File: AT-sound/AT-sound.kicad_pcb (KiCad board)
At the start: 2 copper layers, 17.6 x 17.6 mm, 24 parts, among them J1 PWR, J2 Sound OUT, J3 Sound IN, Q1 AQY212S, U1 ATtiny24-20SSU, U2 SFH617A-2X006, U3 SFH617A-2X006

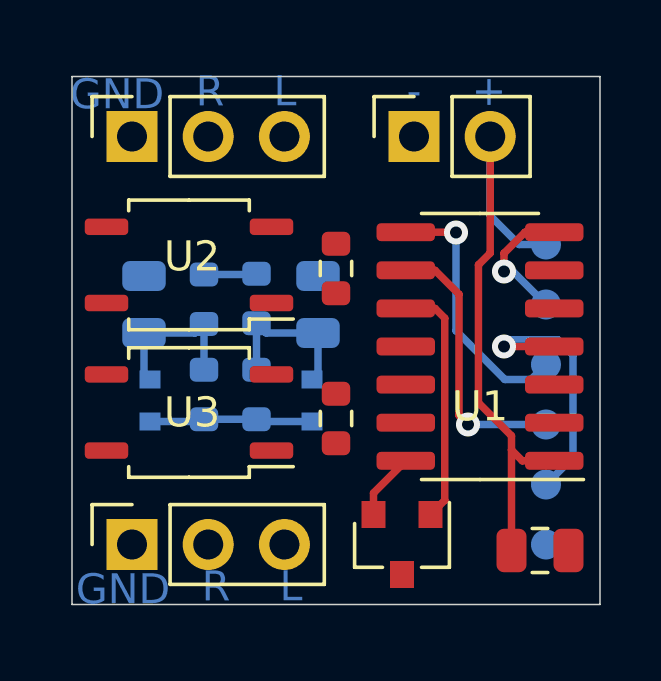
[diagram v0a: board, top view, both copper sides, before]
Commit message: made a external realay verant.
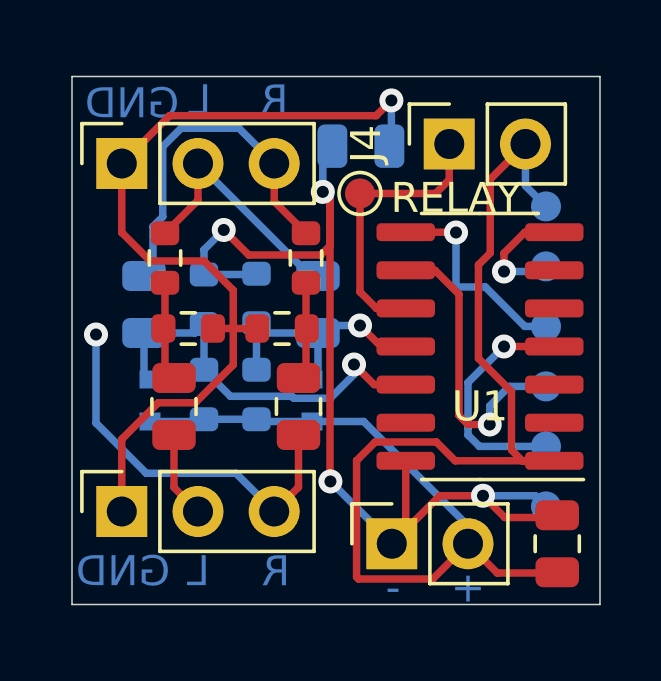
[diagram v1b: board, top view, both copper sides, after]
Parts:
- removed Q1: AQY212S, Package_TO_SOT_SMD:SOT-23
- removed U2, U3: SFH617A-2X006, Package_SO:SOP-4_3.8x4.1mm_P2.54mm
- added C4: 1uF, Capacitor_SMD:C_0805_2012Metric, F.Cu at (161.8, 70.4)
- added C5: 1uF, Capacitor_SMD:C_0805_2012Metric, F.Cu at (157.6, 70.4)
- added C6: 25uF, Capacitor_SMD:C_0805_2012Metric, B.Cu at (163.8, 61.7)
- added J4: PWR, Connector_PinSocket_2.54mm:PinSocket_1x02_P2.54mm_Vertical, F.Cu at (166.8, 61.6)
- added R7: 1K, Resistor_SMD:R_0603_1608Metric, F.Cu at (158.1, 67.8)
- added R8: 1K, Resistor_SMD:R_0603_1608Metric, F.Cu at (161.2, 67.8)
- added TP7: RELAY, TestPoint:TestPoint_Pad_D1.0mm, F.Cu at (163.8, 63.3)
- R5, R6: value 700r -> 27K
- moved J1 13.6 mm to (164.9, 75.0)
- moved J3 12.7 mm to (155.9, 62.3)
- moved J2 12.5 mm to (155.9, 73.9)
- moved R6 7.82 mm to (157.3, 65.5)
- moved TP1 1.27 mm to (170.0, 63.7)
- moved TP2 1.27 mm to (170.0, 73.7)
- moved TP3 1.27 mm to (170.0, 71.7)
- moved TP4 1.27 mm to (170.0, 69.7)
- moved TP5 1.27 mm to (170.0, 67.7)
- moved TP6 1.27 mm to (170.0, 65.7)
- moved R5 1.06 mm to (162.0, 65.5)
- moved C1 0.62 mm to (170.4, 75.0), turned to 90 degrees
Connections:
- J2 pad 1: GND -> Net-(C6-Pad1)
- J3 pad 1: GND -> Net-(C6-Pad1)
- R5 pad 1: Net-(R5-Pad1) -> Net-(C2-Pad1)
- R5 pad 2: Net-(Q1-Pad3) -> Net-(C4-Pad1)
- R6 pad 1: Net-(R6-Pad1) -> Net-(C3-Pad1)
- R6 pad 2: Net-(Q1-Pad3) -> Net-(C5-Pad1)
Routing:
- net GND: track 4.00 -> 35.7 mm, vias 0 -> 4
- net Net-(C6-Pad1): track 0.00 -> 29.3 mm, vias 0 -> 1
- net +5V: track 26.4 -> 46.5 mm
- net Net-(C4-Pad2): track 0.00 -> 13.0 mm, vias 0 -> 1
- net Net-(C2-Pad1): track 0.00 -> 11.8 mm
- net Net-(C3-Pad1): track 0.00 -> 8.33 mm
- net Sense_R: track 5.28 -> 13.3 mm, vias 0 -> 1
- net Sense_L: track 5.37 -> 8.69 mm, vias 0 -> 1
- net Net-(C5-Pad1): track 0.00 -> 3.30 mm
- net Net-(C4-Pad1): track 0.00 -> 3.28 mm
- net Net-(C5-Pad2): track 0.00 -> 2.88 mm
- net Net-(TP5-Pad1): track 8.83 -> 7.04 mm
- net Relay: track 8.18 -> 9.39 mm
- net Net-(TP3-Pad1): track 8.97 -> 7.88 mm
- net Net-(TP4-Pad1): track 9.17 -> 10.1 mm

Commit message: added my smol logo
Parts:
- added REF**: rg-logo-smol, RG:rg-logo-smol, F.Cu at (165.1, 65.5)
- TP3: value RESET -> RE
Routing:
- net (no net): track 0.00 -> 2.57 mm
- net Sense_L: track 8.69 -> 10.1 mm
- net Net-(TP5-Pad1): track 7.04 -> 6.47 mm

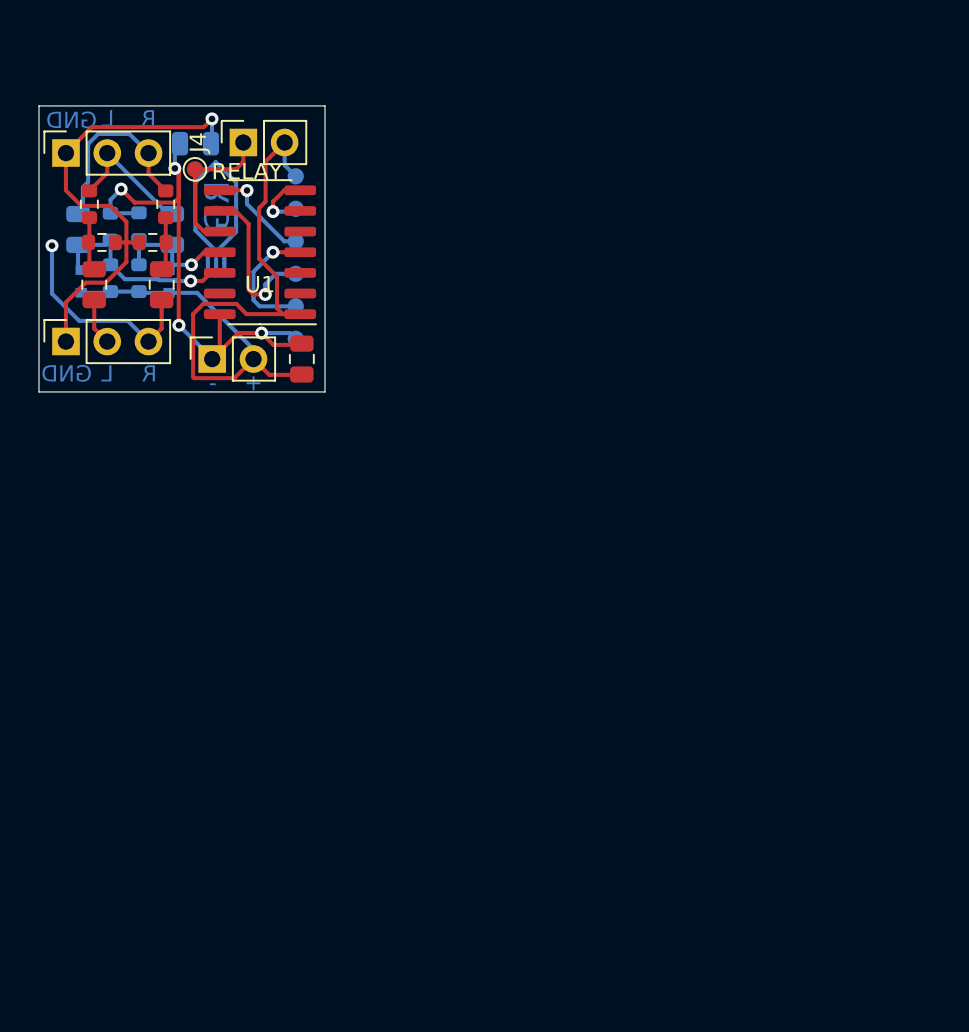
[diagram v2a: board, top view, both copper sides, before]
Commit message: added capacitive dropper cirict for POWERgit add *git add *git add *
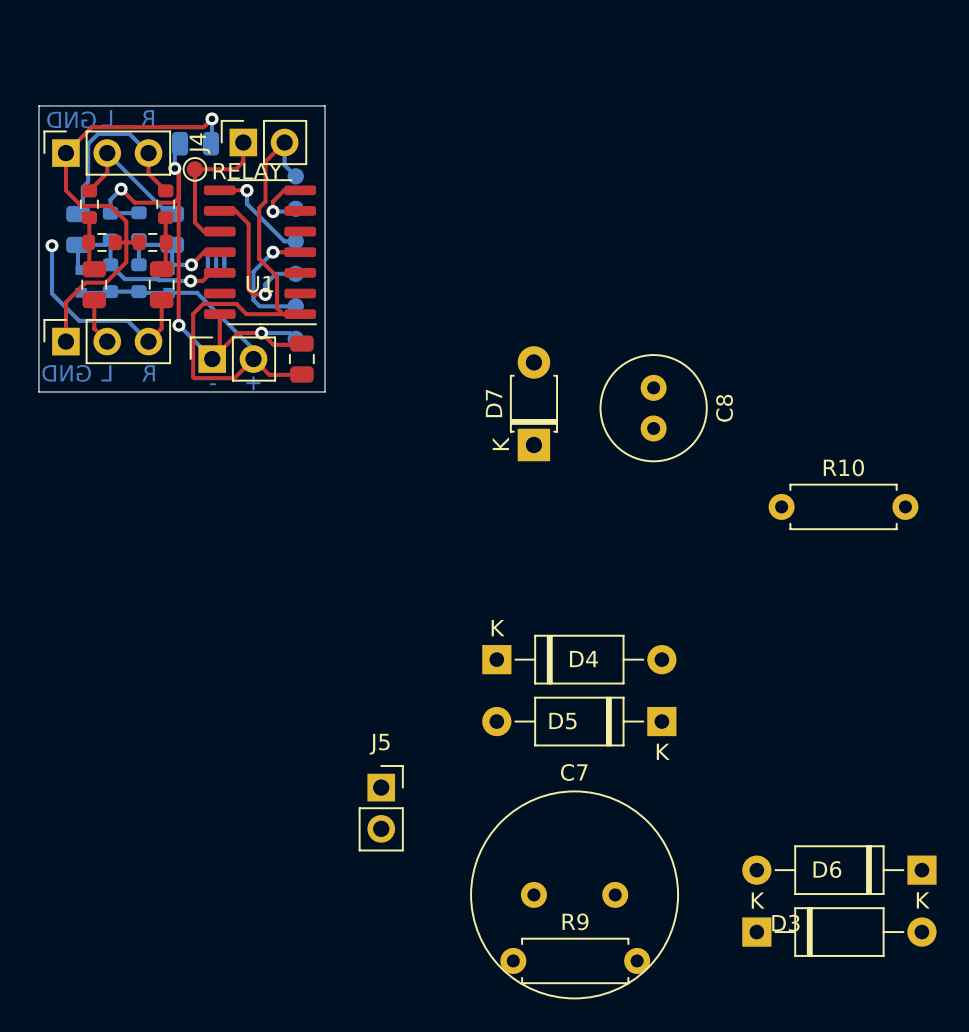
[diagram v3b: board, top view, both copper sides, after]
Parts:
- removed REF**: rg-logo-smol, RG:rg-logo-smol
- added C7: 470nF, Capacitor_THT:C_Radial_D12.5mm_H25.0mm_P5.00mm, F.Cu at (184.7, 108.0)
- added C8: 470uF, Capacitor_THT:C_Radial_D6.3mm_H5.0mm_P2.50mm, F.Cu at (192.0, 76.7)
- added D3: IN4007, Diode_THT:D_A-405_P10.16mm_Horizontal, F.Cu at (198.4, 110.2)
- added D4: IN4007, Diode_THT:D_A-405_P10.16mm_Horizontal, F.Cu at (182.4, 93.5)
- added D5: IN4007, Diode_THT:D_A-405_P10.16mm_Horizontal, F.Cu at (192.5, 97.3)
- added D6: IN4007, Diode_THT:D_A-405_P10.16mm_Horizontal, F.Cu at (208.5, 106.4)
- added D7: D_Zener_ALT, Diode_THT:D_T-1_P5.08mm_Horizontal, F.Cu at (184.7, 80.3)
- added J5: MAINS, Connector_PinSocket_2.54mm:PinSocket_1x02_P2.54mm_Vertical, F.Cu at (175.3, 101.3)
- added R10: 100r, Resistor_THT:R_Axial_DIN0207_L6.3mm_D2.5mm_P7.62mm_Horizontal, F.Cu at (199.9, 84.1)
- added R9: 1M, Resistor_THT:R_Axial_DIN0207_L6.3mm_D2.5mm_P7.62mm_Horizontal, F.Cu at (183.4, 112.0)
- TP3: value RE -> RESET

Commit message: did a little layout for capacitve dropper
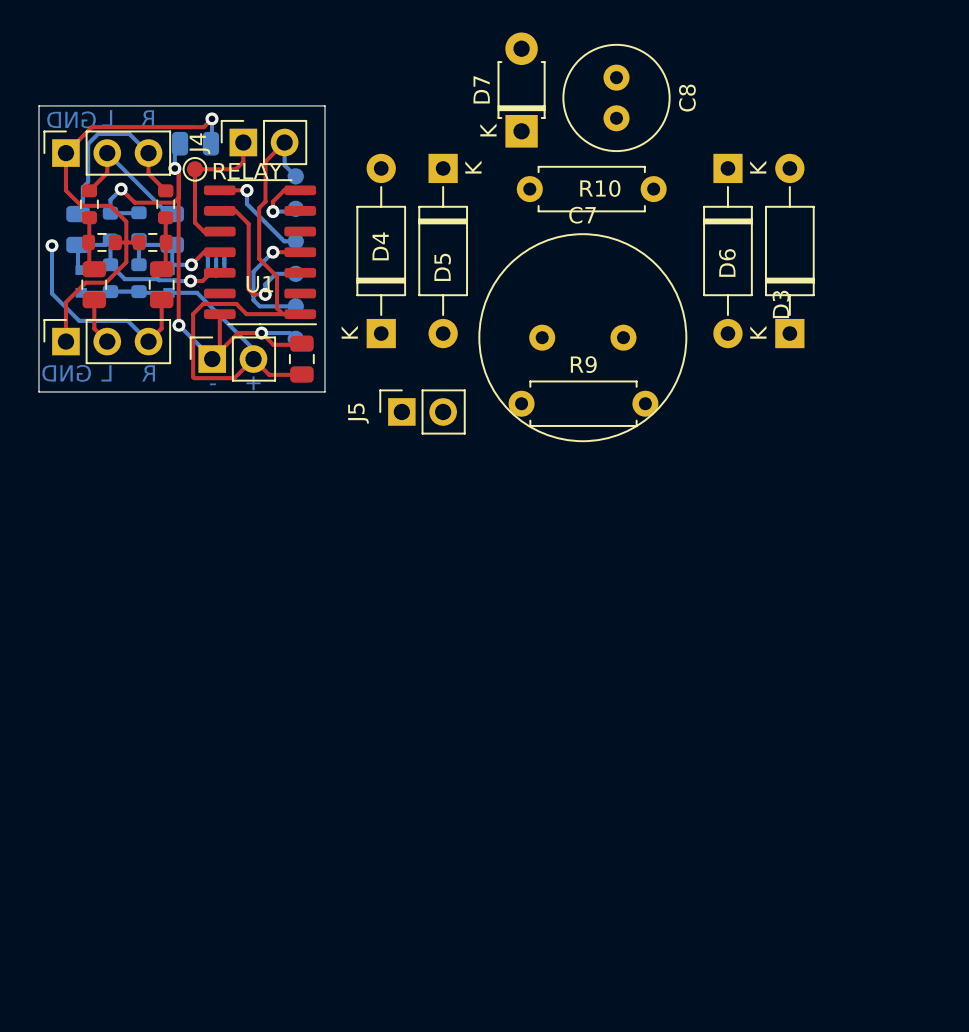
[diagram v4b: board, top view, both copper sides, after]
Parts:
- moved D6 44.8 mm to (196.6, 63.2), turned to 270 degrees
- moved D3 36.9 mm to (200.4, 73.4), turned to 90 degrees
- moved D5 36.6 mm to (179.1, 63.2), turned to 270 degrees
- moved C7 34.3 mm to (185.2, 73.7)
- moved R9 34.3 mm to (183.9, 77.7)
- moved R10 25.0 mm to (184.4, 64.5)
- moved J5 23.1 mm to (176.5, 78.2), turned to 90 degrees
- moved D4 21.3 mm to (175.3, 73.4), turned to 90 degrees
- moved D7 19.3 mm to (183.9, 61.0)
- moved C8 19.2 mm to (189.7, 57.7)
